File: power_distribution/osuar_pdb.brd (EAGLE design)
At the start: 42.9 x 53.3 mm, 27 parts, among them J1 M02, J2 M02, J3 M02, J4 M02, J5 M02, J6 M02, J7 M02, J8 M02

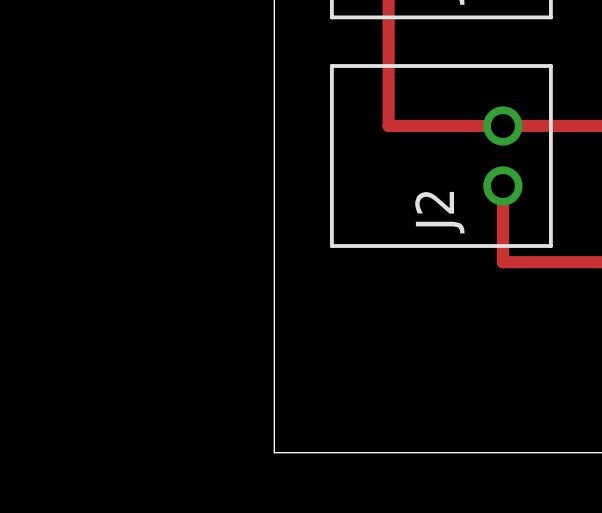
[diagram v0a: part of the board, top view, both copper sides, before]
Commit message: Add extra Vin connector to pdb schematic
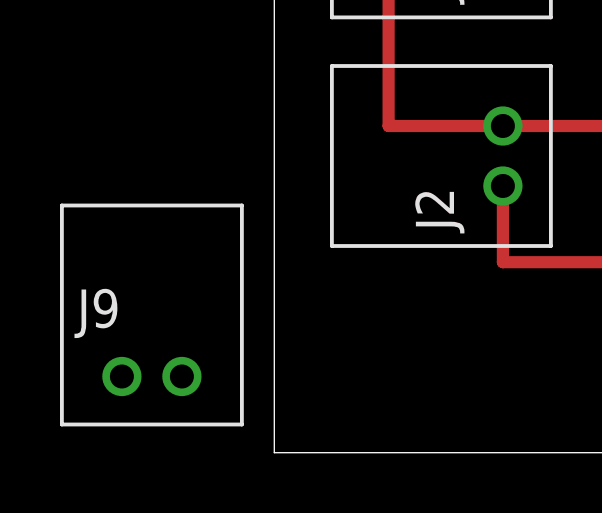
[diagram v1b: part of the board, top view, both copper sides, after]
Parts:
- added J9: M02, OSURC_Connectors:MOLEX-2MM-MICROLATCH-2POS-RA
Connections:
- net GND: now also J9.2
- net VCC: now also J9.1
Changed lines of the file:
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@@
 <?xml version="1.0" encoding="utf-8"?>
 <!DOCTYPE eagle SYSTEM "eagle.dtd">
-<eagle version="7.1.0">
+<eagle version="6.5.0">
 <drawing>
 <settings>
@@
 <pass name="Default">
 <param name="RoutingGrid" value="50mil"/>
-<param name="AutoGrid" value="1"/>
-<param name="Efforts" value="0"/>
-<param name="TopRouterVariant" value="1"/>
 <param name="tpViaShape" value="round"/>
 <param name="PrefDir.1" value="|"/>
@@
 <element name="J8" library="OSURC_Connectors" package="MOLEX-2MM-MICROLATCH-2POS-RA" value="M02" x="10.16" y="74.93" rot="R90">
 <attribute name="DIGIKEY_PN" value="WM18999-ND" x="49.53" y="92.71" size="1.778" layer="27" rot="R90" display="off"/>
+</element>
+<element name="J9" library="OSURC_Connectors" package="MOLEX-2MM-MICROLATCH-2POS-RA" value="M02" x="-2.54" y="30.48">
+<attribute name="DIGIKEY_PN" value="WM18999-ND" x="-2.54" y="30.48" size="1.778" layer="27" display="off"/>
 </element>
 </elements>
@@
 <contactref element="R4" pad="2"/>
 <contactref element="J1" pad="2"/>
+<contactref element="J9" pad="2"/>
 <wire x1="30.48" y1="73.67" x2="38.1" y2="74.537" width="0" layer="19" extent="1-1"/>
 <wire x1="30.48" y1="73.66" x2="30.48" y2="73.67" width="0" layer="19" extent="1-1"/>
@@
 <wire x1="26.67" y1="50.43" x2="26.67" y2="52.463" width="0" layer="19" extent="1-1"/>
 <wire x1="15.23" y1="55.88" x2="15.23" y2="53.34" width="0" layer="19" extent="1-1"/>
+<wire x1="-0.54" y1="30.48" x2="6.35" y2="38.83" width="0" layer="19" extent="1-1"/>
 </signal>
 <signal name="N$3">
@@
 <contactref element="U$4" pad="7"/>
 <contactref element="C7" pad="2"/>
+<contactref element="J9" pad="1"/>
 <wire x1="21.59" y1="71.755" x2="24.34" y2="71.755" width="0" layer="19" extent="1-1"/>
 <wire x1="24.13" y1="63.87" x2="24.13" y2="63.5" width="0" layer="19" extent="1-1"/>
@@
 <wire x1="20.53" y1="50.165" x2="17.78" y2="55.88" width="0" layer="19" extent="1-16"/>
 <wire x1="24.13" y1="48.63" x2="20.53" y2="50.165" width="0" layer="19" extent="1-1"/>
+<wire x1="-2.54" y1="30.48" x2="20.53" y2="50.165" width="0" layer="19" extent="1-1"/>
 </signal>
 <signal name="N$5">
